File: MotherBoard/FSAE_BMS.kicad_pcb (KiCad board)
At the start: 2 copper layers, 197 parts, among them IC501 BQ79600PWRQ1, J201 Conn_ARM_SWD_TagConnect_TC2030, J202 DM3AT-SF-PEJM5_40_, J301 1376357-3, J302 Conn_01x04_Pin, J303 430450200, Q701 Q_NMOS_GDS, Q702 Q_NPN_BEC, Q703 Q_NPN_BEC, Q704 Q_NMOS_GDS, Q705 Q_NPN_BEC, Q706 Q_NMOS_GDS, Q708 Q_NPN_BEC, Q709 Q_NMOS_GDS, U201 STM32F205RBTx, U401 LMR51430, U402 LMR51430, U601 PTCAN1462DRQ1, U602 PTCAN1462DRQ1, Y201 16 Mhz

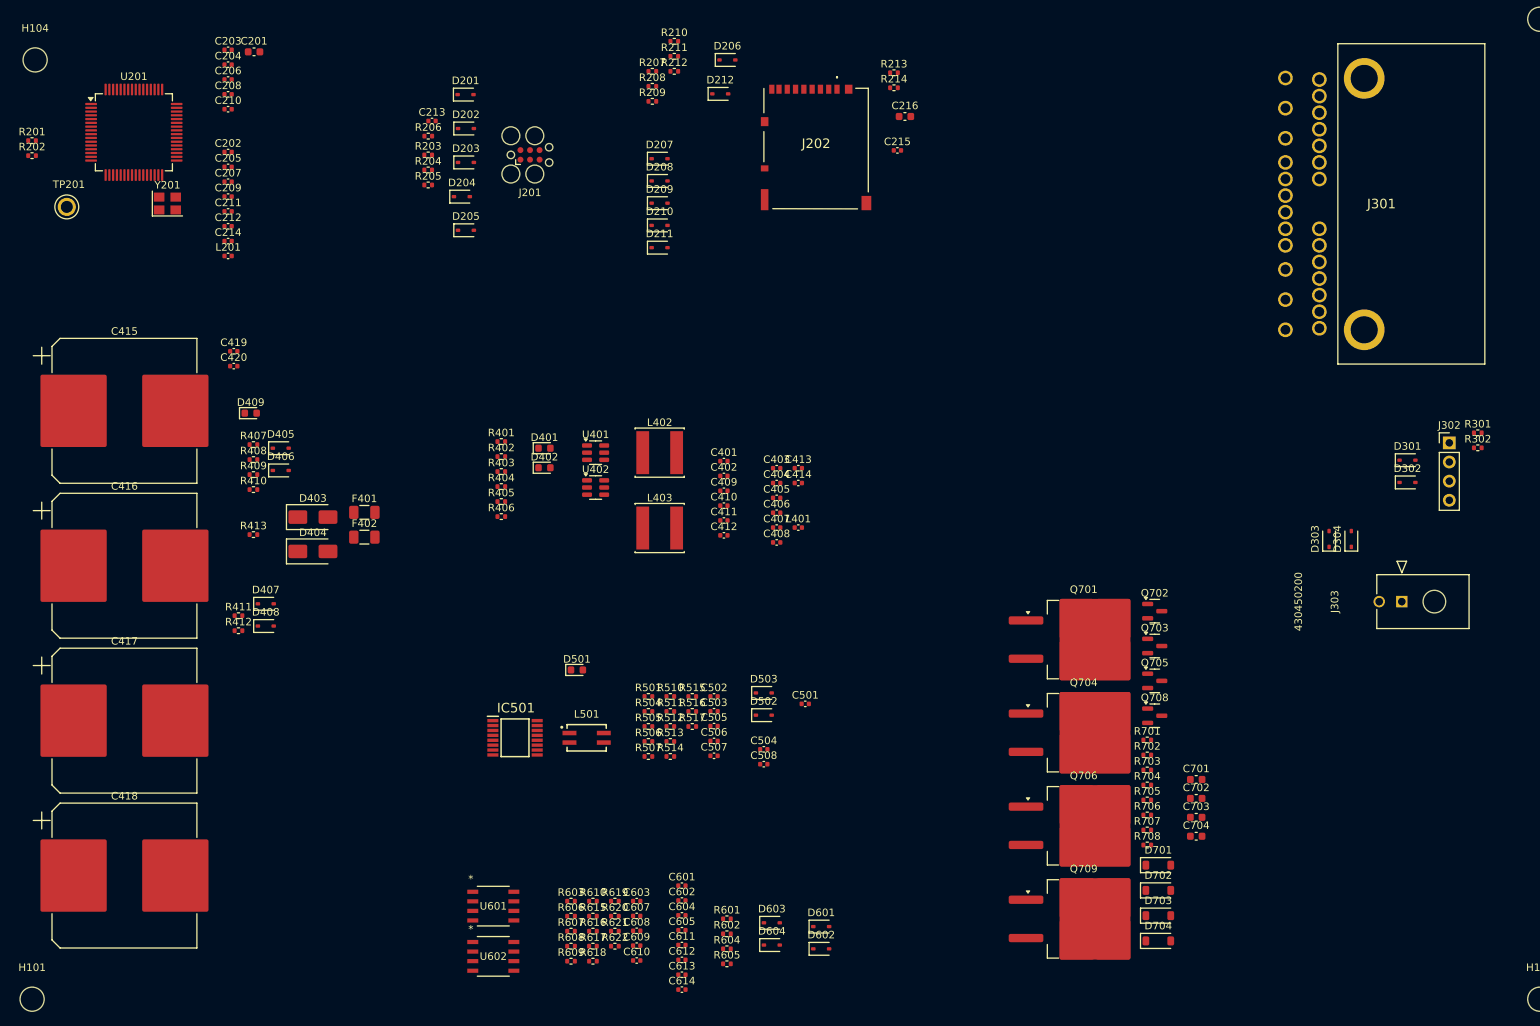
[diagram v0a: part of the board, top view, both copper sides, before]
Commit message: Completed BOM except inductors
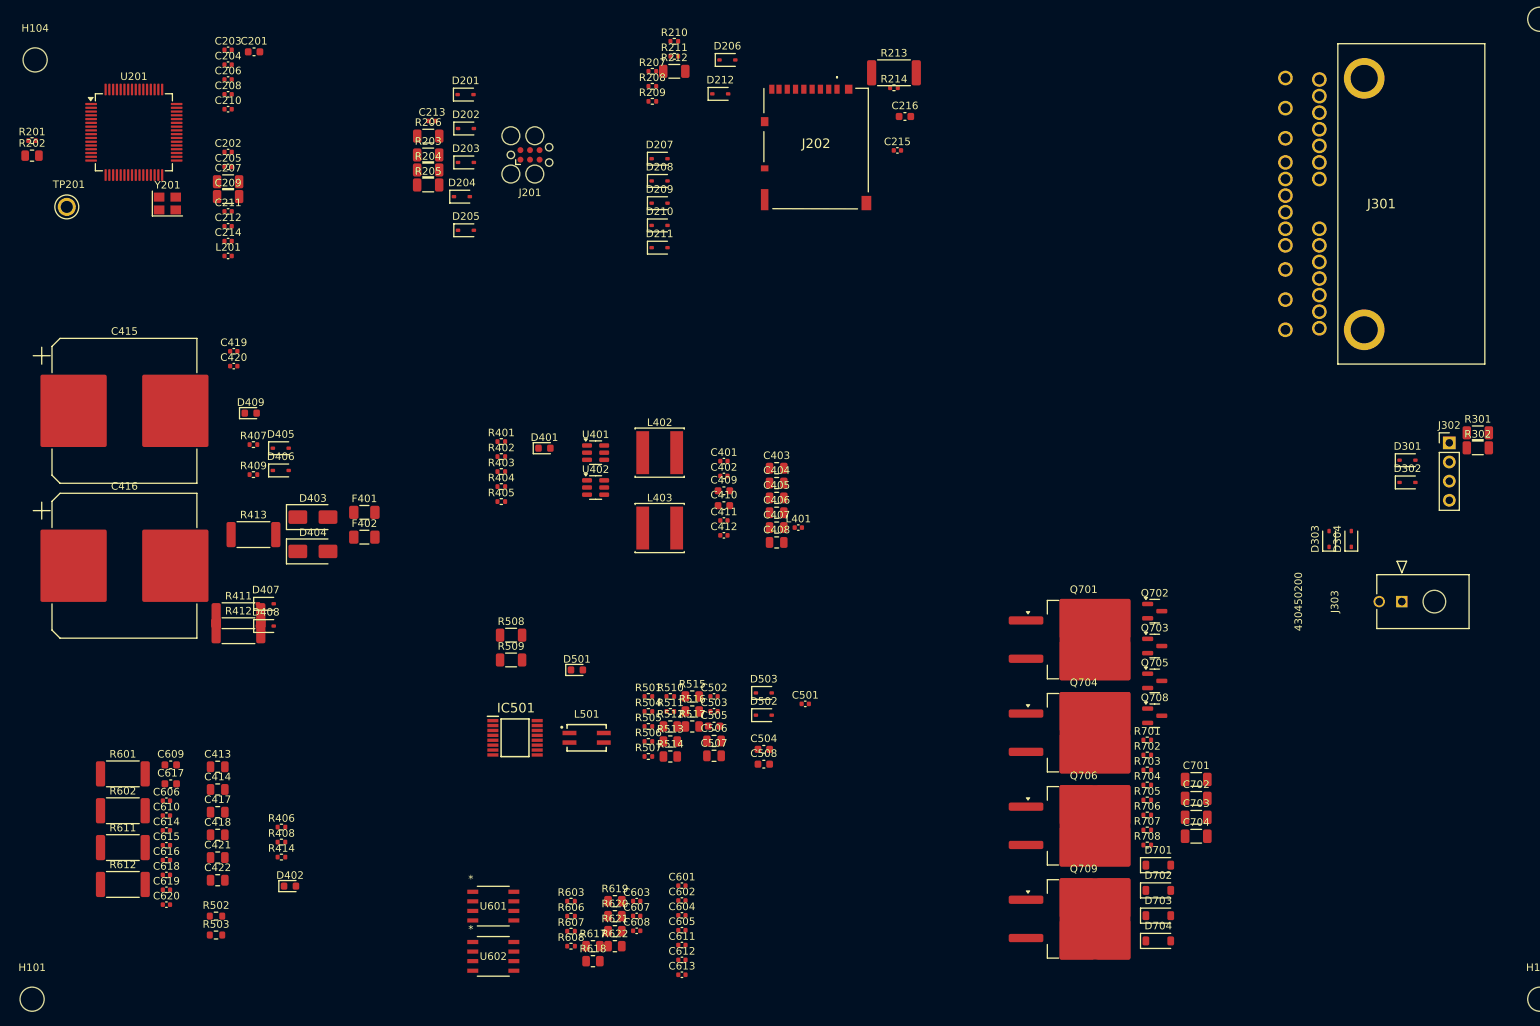
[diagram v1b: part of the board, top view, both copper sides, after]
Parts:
- removed D601, D602, D603, D604: D_TVS, Diode_SMD:D_SOD-323
- removed R410: 33k, Resistor_SMD:R_0402_1005Metric
- removed R604, R605: 0R, Resistor_SMD:R_0402_1005Metric
- removed R609, R610, R615, R616: 10k, Resistor_SMD:R_0402_1005Metric
- added C421: 22u, Capacitor_SMD:C_0805_2012Metric, F.Cu at (49.6, 131.2)
- added C422: 22u, Capacitor_SMD:C_0805_2012Metric, F.Cu at (49.6, 134.2)
- added C606: 4.7n, Capacitor_SMD:C_0402_1005Metric, F.Cu at (42.8, 123.7)
- added C615: 20pf, Capacitor_SMD:C_0402_1005Metric, F.Cu at (42.8, 129.6)
- added C616: 20pf, Capacitor_SMD:C_0402_1005Metric, F.Cu at (42.8, 131.6)
- added C617: 10u, Capacitor_SMD:C_0603_1608Metric, F.Cu at (43.4, 121.4)
- added C618: 1u, Capacitor_SMD:C_0402_1005Metric, F.Cu at (42.8, 133.5)
- added C619: 1u, Capacitor_SMD:C_0402_1005Metric, F.Cu at (42.8, 135.5)
- added C620: 1u, Capacitor_SMD:C_0402_1005Metric, F.Cu at (42.8, 137.5)
- added R414: 33k, Resistor_SMD:R_0402_1005Metric, F.Cu at (58.1, 131.2)
- added R502: 499, Resistor_SMD:R_0603_1608Metric, F.Cu at (49.4, 139.0)
- added R503: 499, Resistor_SMD:R_0603_1608Metric, F.Cu at (49.4, 141.5)
- added R508: 51, Resistor_SMD:R_1206_3216Metric, F.Cu at (88.5, 101.7)
- added R509: 51, Resistor_SMD:R_1206_3216Metric, F.Cu at (88.5, 105.0)
- added R611: 60.4, Resistor_SMD:R_2512_6332Metric, F.Cu at (37.0, 129.9)
- added R612: 60.4, Resistor_SMD:R_2512_6332Metric, F.Cu at (37.0, 134.8)
- C207, C209: footprint Capacitor_SMD:C_0402_1005Metric -> Resistor_SMD:R_1206_3216Metric
- C403, C404, C405, C406, C407, C408, C506, C507: footprint Capacitor_SMD:C_0402_1005Metric -> Capacitor_SMD:C_0805_2012Metric
- C409, C410, C505: footprint Capacitor_SMD:C_0402_1005Metric -> Capacitor_SMD:C_0603_1608Metric
- C413, C414: value 47u -> 22u; footprint Capacitor_SMD:C_0402_1005Metric -> Capacitor_SMD:C_0805_2012Metric
- C415, C416: value 3300u -> 2200u
- C417, C418: value 3300u -> 22u; footprint Capacitor_SMD:CP_Elec_18x17.5 -> Capacitor_SMD:C_0805_2012Metric
- C504, C508: value 100n -> 220n; footprint Capacitor_SMD:C_0402_1005Metric -> Capacitor_SMD:C_0603_1608Metric
- C601, C602, C604, C605: value 100n -> 20p
- C609: value 20pf -> 10u; footprint Capacitor_SMD:C_0402_1005Metric -> Capacitor_SMD:C_0603_1608Metric
- C610: value 20pf -> 1u
- C701, C702, C703, C704: footprint Capacitor_SMD:C_0603_1608Metric -> Capacitor_SMD:C_1206_3216Metric
- L402, L403: value 22u -> 10u
- R202, R512, R513, R514, R515, R516, R517, R617, R618, R619, R620, R621, R622: footprint Resistor_SMD:R_0402_1005Metric -> Resistor_SMD:R_0805_2012Metric
- R203, R204, R205, R206, R212, R301, R302: footprint Resistor_SMD:R_0402_1005Metric -> Resistor_SMD:R_1206_3216Metric
- R213, R411, R412: footprint Resistor_SMD:R_0402_1005Metric -> Resistor_SMD:R_2512_6332Metric
- R413: value 1K -> 1k; footprint Resistor_SMD:R_0402_1005Metric -> Resistor_SMD:R_2512_6332Metric
- R601, R602: value 0R -> 60.4; footprint Resistor_SMD:R_0402_1005Metric -> Resistor_SMD:R_2512_6332Metric
- moved C414 87.1 mm to (49.6, 122.2)
- moved C413 86.6 mm to (49.6, 119.2)
- moved R601 82.4 mm to (37.0, 120.1)
- moved R602 81.8 mm to (37.0, 125.0)
- moved C614 71.6 mm to (42.8, 127.6)
- moved C609 66.3 mm to (43.4, 118.9)
- moved C610 65.3 mm to (42.8, 125.6)
- moved D402 65.0 mm to (59.2, 135.0)
- moved R408 50.9 mm to (58.1, 129.2)
- moved R406 50.5 mm to (58.1, 127.2)
- moved C417 17.3 mm to (49.6, 125.2)
- moved C418 13.5 mm to (49.6, 128.2)
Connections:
- C414 pad 1: +5V -> +3V3
- C417 pad 1: VBUS -> +5V
- C418 pad 1: VBUS -> +5V
- C419 pad 1: Net-(C419-Pad1) -> /PSU/READY_PWR_LV
- C420 pad 1: Net-(C420-Pad1) -> /PSU/CHARGE_PWR_LV
- C609 pad 1: GND -> +5V
- C609 pad 2: ISO_CAN2+ -> GND
- C610 pad 1: ISO_CAN2- -> +5V
- D409 pad 1: GND -> Net-(D409-K)
- R408 pad 1: /PSU/READY_PWR_LV -> /PSU/CHARGE_PWR_LV
- R408 pad 2: Net-(C419-Pad1) -> GND
- R413 pad 1: GND -> Net-(D409-K)
- R601 pad 1: ISO_CAN1+ -> Net-(C606-Pad1)
- R601 pad 2: /TCAN1462-Q1/CANH_1 -> ISO_CAN2+
- R602 pad 1: ISO_CAN1- -> ISO_CAN2-
- R602 pad 2: /TCAN1462-Q1/CANL_1 -> Net-(C606-Pad1)
- U601 pad 6: /TCAN1462-Q1/CANL_1 -> ISO_CAN1-
- U601 pad 7: /TCAN1462-Q1/CANH_1 -> ISO_CAN1+
- U602 pad 6: /TCAN1462-Q1/CANL_2 -> ISO_CAN2-
- U602 pad 7: /TCAN1462-Q1/CANH_2 -> ISO_CAN2+

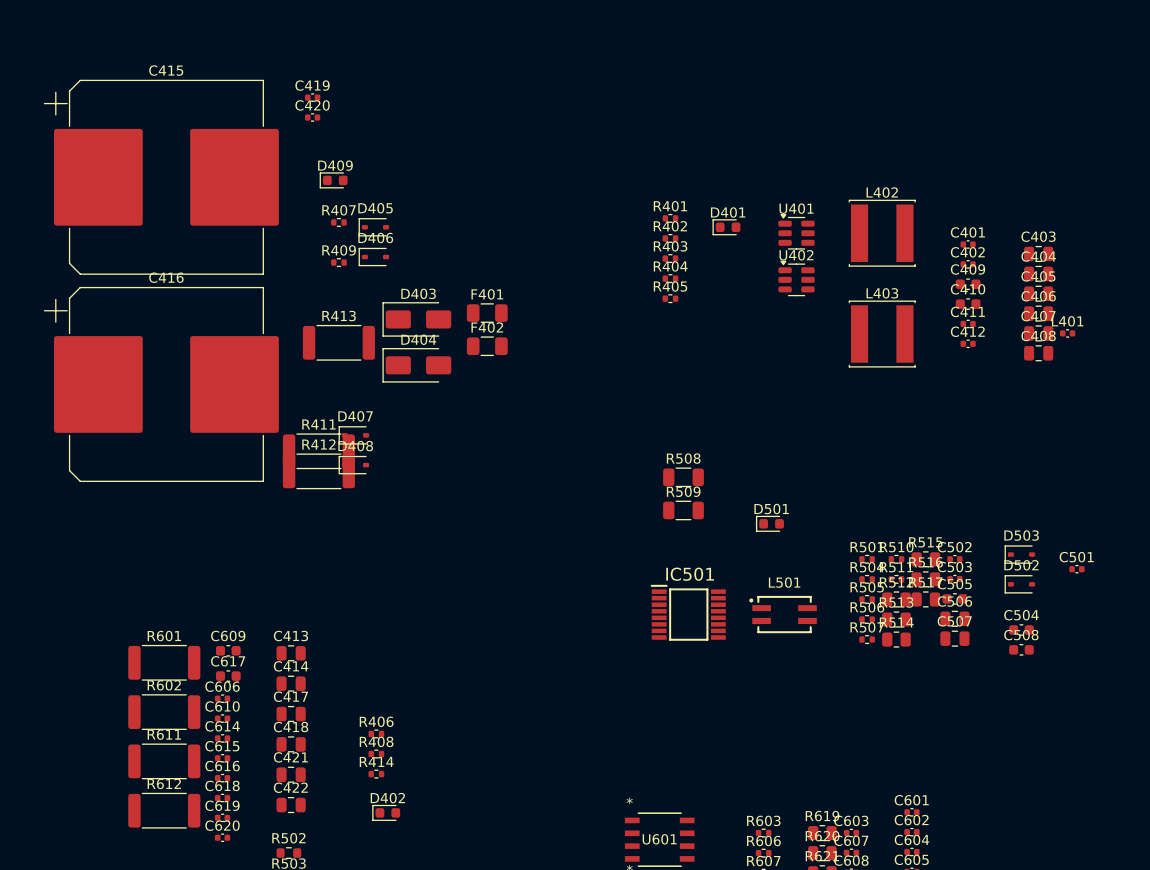
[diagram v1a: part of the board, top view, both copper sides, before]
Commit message: Redesigned EMI filters for switching regulators to meet CISPR 25 Class 5 EMI constraint + substituted BOM #s for JLC basic parts
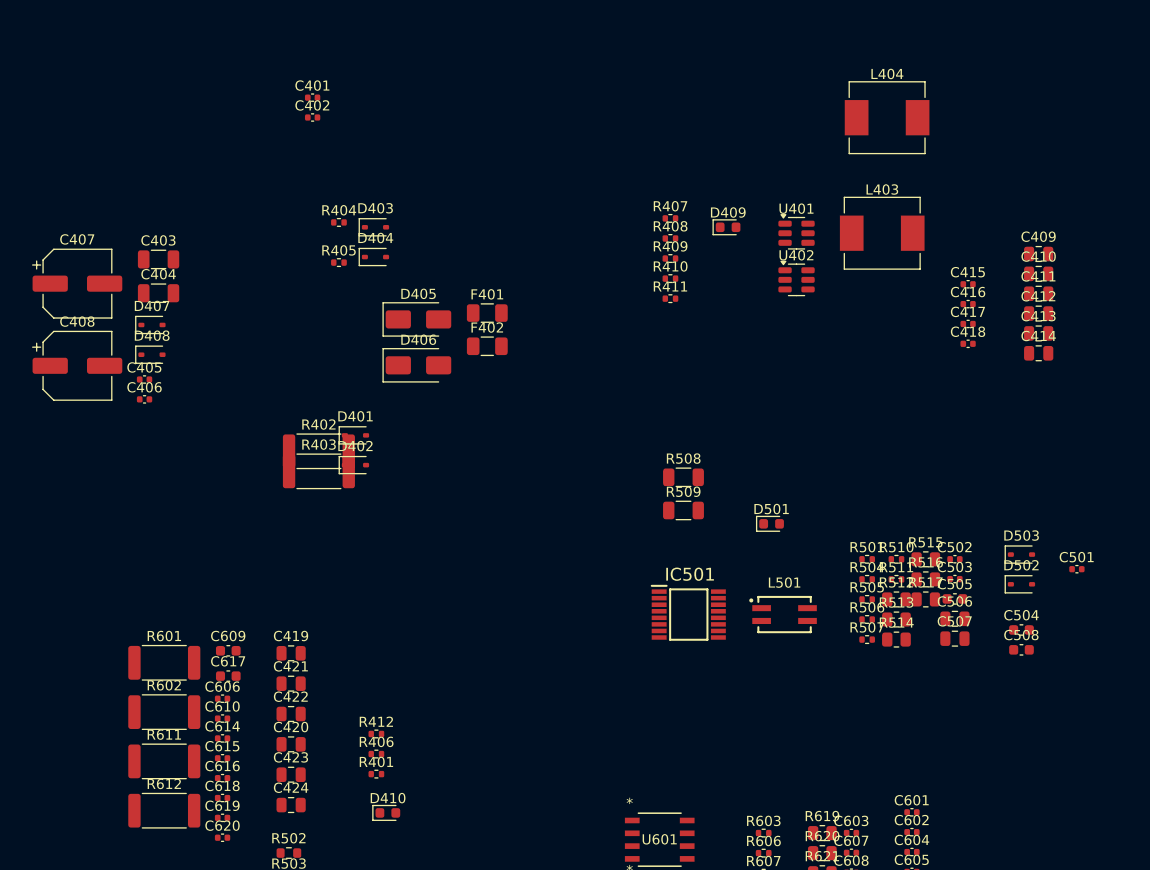
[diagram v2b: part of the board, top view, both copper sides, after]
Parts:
- removed the C401 at (116.8, 78.6)
- removed the C402 at (116.8, 80.6)
- removed the C415 at (37.2, 72.0)
- removed the C416 at (37.2, 92.5)
- removed the D409 at (54.0, 72.3)
- removed L401: 10n, Capacitor_SMD:C_0402_1005Metric
- removed the L403 at (108.2, 87.5)
- removed R413: 1k, Resistor_SMD:R_2512_6332Metric
- added C403: 4.7u, Capacitor_SMD:C_1206_3216Metric, F.Cu at (36.5, 80.1)
- added C404: 4.7u, Capacitor_SMD:C_1206_3216Metric, F.Cu at (36.5, 83.5)
- added C405: 100n, Capacitor_SMD:C_0402_1005Metric, F.Cu at (35.1, 92.0)
- added C406: 100n, Capacitor_SMD:C_0402_1005Metric, F.Cu at (35.1, 94.0)
- added C407: 100u, Capacitor_SMD:CP_Elec_6.3x5.8, F.Cu at (28.4, 82.5)
- added C408: 100u, Capacitor_SMD:CP_Elec_6.3x5.8, F.Cu at (28.4, 90.7)
- added D407: D_TVS, Diode_SMD:D_SOD-323, F.Cu at (35.8, 86.6)
- added D408: D_TVS, Diode_SMD:D_SOD-323, F.Cu at (35.8, 89.5)
- added L404: 10u, Inductor_SMD:L_Sunlord_MWSA0603S, F.Cu at (108.7, 66.0)
- C415: renamed from C409; footprint Capacitor_SMD:C_0603_1608Metric -> Capacitor_SMD:C_0402_1005Metric
- C416: renamed from C410; footprint Capacitor_SMD:C_0603_1608Metric -> Capacitor_SMD:C_0402_1005Metric
- L403: renamed from L402; footprint Inductor_SMD:L_Changjiang_FNR6045S -> Inductor_SMD:L_Sunlord_MWSA0603S
- renumbered C419 to C401, C420 to C402, C403 to C409, C404 to C410, C405 to C411, C406 to C412, C407 to C413, C408 to C414, C411 to C417, C412 to C418, C413 to C419, C418 to C420, C414 to C421, C417 to C422, C421 to C423, C422 to C424, D407 to D401, D408 to D402, D405 to D403, D406 to D404, D403 to D405, D404 to D406, D401 to D409, D402 to D410, R414 to R401, R411 to R402, R412 to R403, R407 to R404, R409 to R405, R408 to R406, R401 to R407, R402 to R408, R403 to R409, R404 to R410, R405 to R411, R406 to R412
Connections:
- C409 pad 1: +12V -> Net-(D407-A2)
- C410 pad 1: +12V -> Net-(D408-A2)
- C411 pad 1: +12V -> Net-(D407-A2)
- C412 pad 1: +12V -> Net-(D408-A2)
- C413 pad 1: +12V -> Net-(D407-A2)
- C414 pad 1: +12V -> Net-(D408-A2)
- C415 pad 1: +12V -> Net-(D407-A2)
- C416 pad 1: +12V -> Net-(D408-A2)
- U401 pad 3: +12V -> Net-(D407-A2)
- U401 pad 5: +12V -> Net-(D407-A2)
- U402 pad 3: +12V -> Net-(D408-A2)
- U402 pad 5: +12V -> Net-(D408-A2)
